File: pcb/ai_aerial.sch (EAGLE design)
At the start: 33 parts

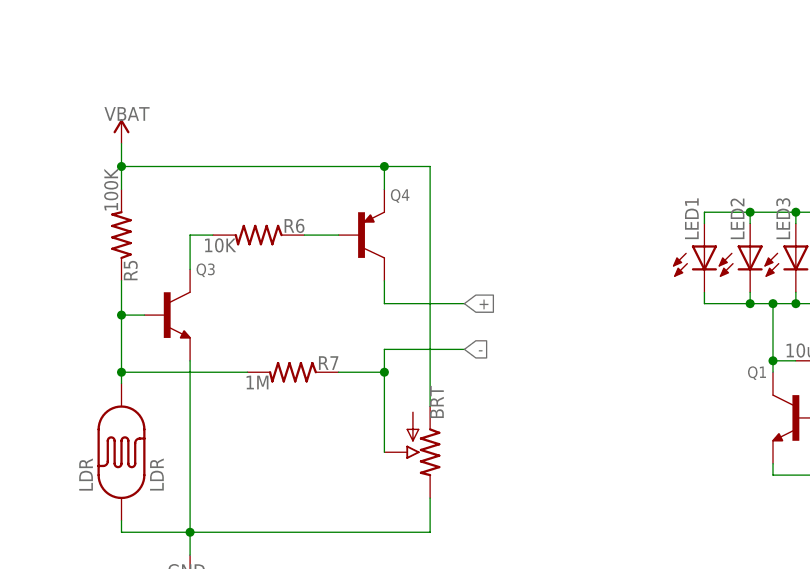
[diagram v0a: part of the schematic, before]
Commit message: fixing trace error
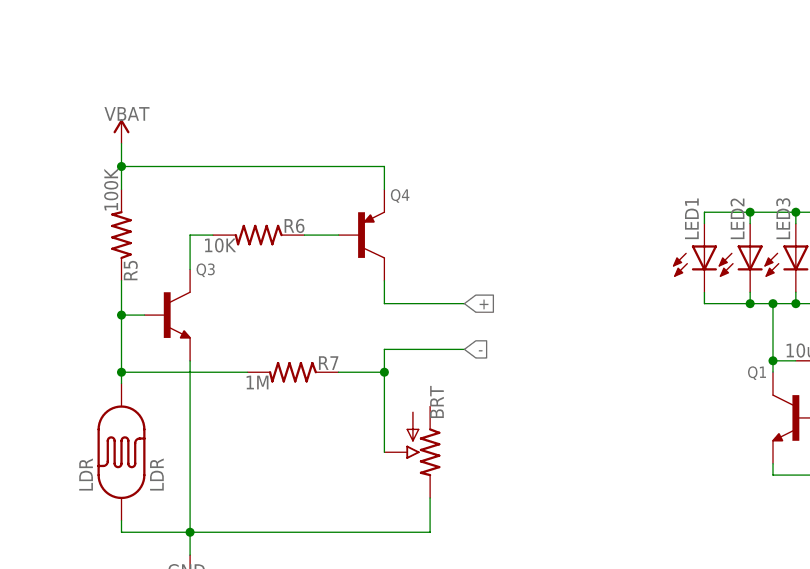
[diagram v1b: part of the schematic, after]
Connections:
- net VBAT: no longer BRT.A
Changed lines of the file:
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@@
 <?xml version="1.0" encoding="utf-8"?>
 <!DOCTYPE eagle SYSTEM "eagle.dtd">
-<eagle version="7.1.0">
+<eagle version="6.5.0">
 <drawing>
 <settings>
@@
 <wire x1="76.2" y1="87.63" x2="105.41" y2="87.63" width="0.1524" layer="91"/>
 <wire x1="105.41" y1="87.63" x2="105.41" y2="85.09" width="0.1524" layer="91"/>
-<pinref part="BRT" gate="G$1" pin="A"/>
-<wire x1="105.41" y1="87.63" x2="110.49" y2="87.63" width="0.1524" layer="91"/>
-<wire x1="110.49" y1="87.63" x2="110.49" y2="60.96" width="0.1524" layer="91"/>
-<junction x="105.41" y="87.63"/>
 <pinref part="U$2" gate="G$1" pin="VBAT"/>
 <wire x1="76.2" y1="87.63" x2="76.2" y2="90.17" width="0.1524" layer="91"/>
